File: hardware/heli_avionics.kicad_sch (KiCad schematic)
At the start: 17 parts, among them J1 Pin_Header_2x3, J7 JST_ZH_01x02, SW1 Reset, U1 ATmega4808-A

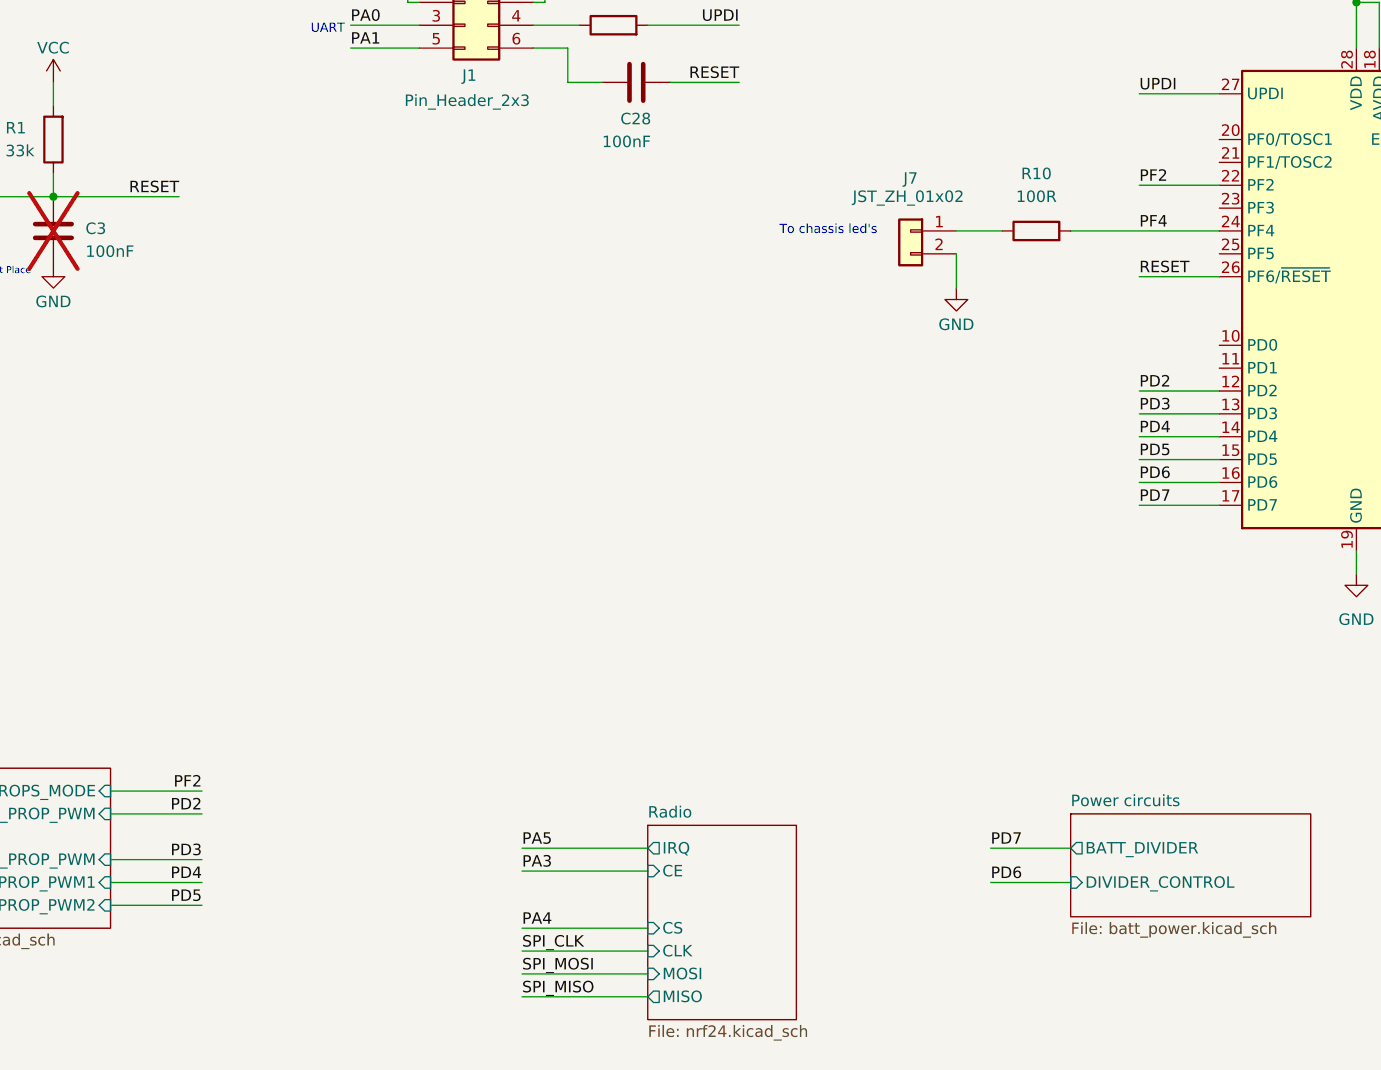
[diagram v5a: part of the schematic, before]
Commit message: Reordered some MCU pin connections for nicer layout
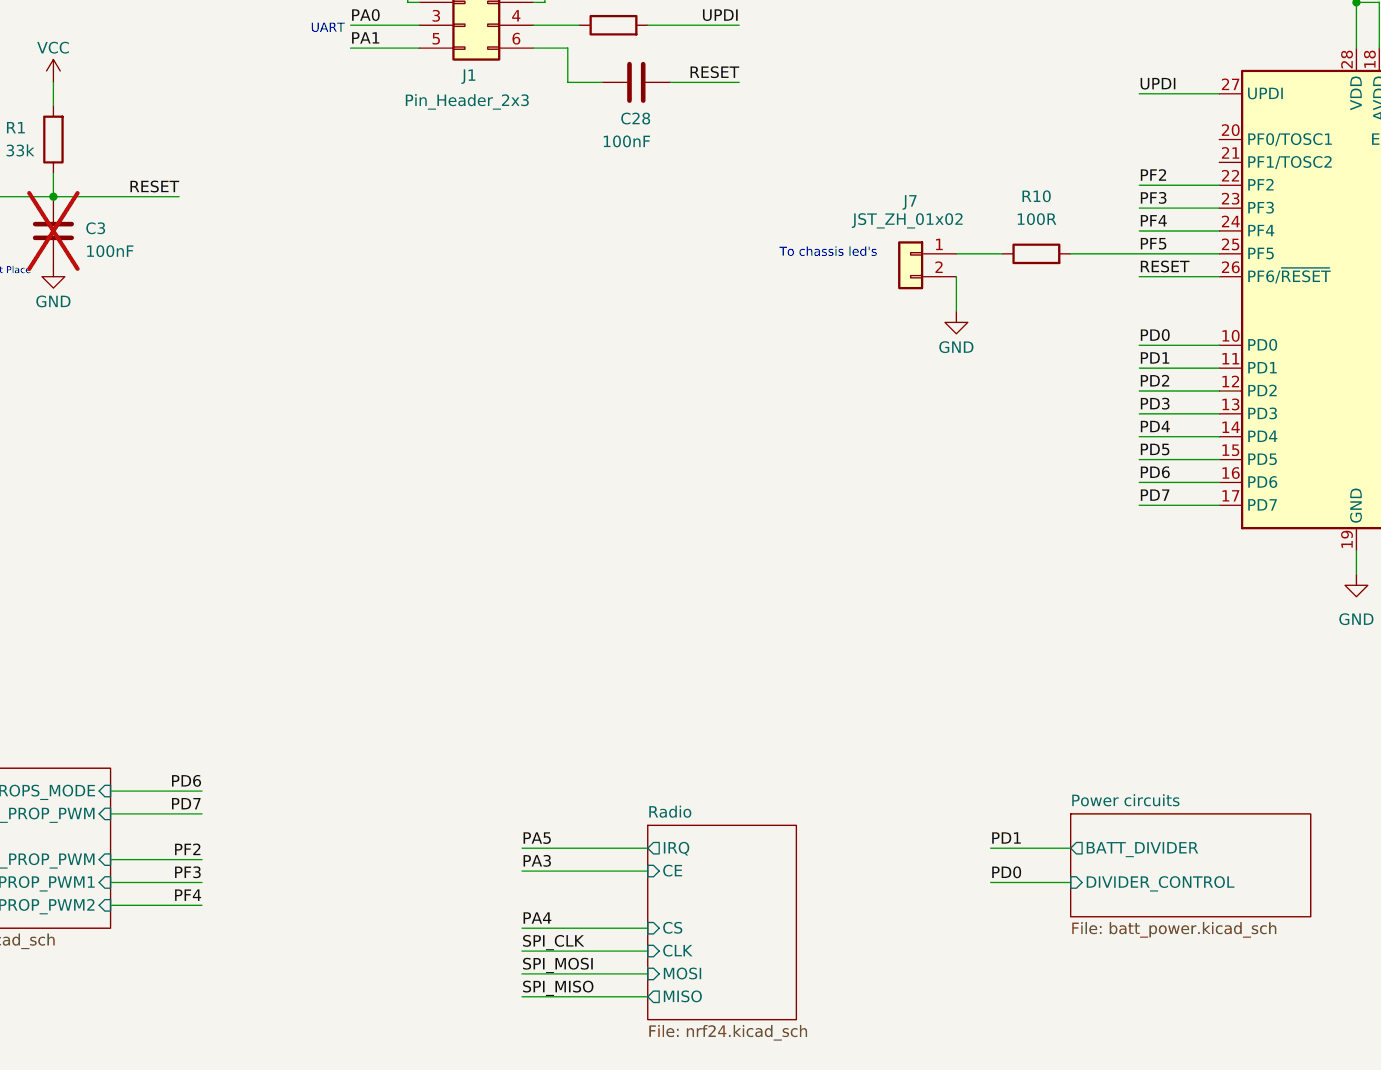
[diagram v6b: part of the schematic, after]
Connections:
- net PF4: no longer R10.2
- net PD0: now reaches U1.10 (PD0)
- net PD1: now reaches U1.11 (PD1)
- net PF3: now reaches U1.23 (PF3)
- net PF5: now reaches U1.25 (PF5)
- net PF5: now also R10.2
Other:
- moved on the sheet: J7, R10
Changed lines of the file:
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@@
+	(wire
+		(pts
+			(xy 181.61 68.58) (xy 190.5 68.58)
+		)
+		(stroke
+			(width 0)
+			(type default)
+		)
+	)
 	(wire
 		(pts
@@
 	(wire
 		(pts
+			(xy 181.61 83.82) (xy 190.5 83.82)
+		)
+		(stroke
+			(width 0)
+			(type default)
+		)
+	)
+	(wire
+		(pts
 			(xy 205.74 39.37) (xy 205.74 43.18)
 		)
@@
 	(wire
 		(pts
+			(xy 173.99 71.12) (xy 190.5 71.12)
+		)
+		(stroke
+			(width 0)
+			(type default)
+		)
+	)
+	(wire
+		(pts
 			(xy 68.58 180.34) (xy 81.28 180.34)
 		)
@@
 	(wire
 		(pts
+			(xy 181.61 66.04) (xy 190.5 66.04)
+		)
+		(stroke
+			(width 0)
+			(type default)
+		)
+	)
+	(wire
+		(pts
 			(xy 29.21 64.77) (xy 29.21 69.85)
 		)
@@
 	(wire
 		(pts
-			(xy 161.29 68.58) (xy 166.37 68.58)
+			(xy 161.29 71.12) (xy 166.37 71.12)
 		)
 		(stroke
@@
 	(wire
 		(pts
+			(xy 181.61 81.28) (xy 190.5 81.28)
+		)
+		(stroke
+			(width 0)
+			(type default)
+		)
+	)
+	(wire
+		(pts
 			(xy 205.74 43.18) (xy 208.28 43.18)
 		)
@@
 	(wire
 		(pts
-			(xy 161.29 71.12) (xy 161.29 74.93)
+			(xy 161.29 73.66) (xy 161.29 77.47)
 		)
 		(stroke
@@
 		(pts
 			(xy 181.61 96.52) (xy 190.5 96.52)
-		)
-		(stroke
-			(width 0)
-			(type default)
-		)
-	)
-	(wire
-		(pts
-			(xy 173.99 68.58) (xy 190.5 68.58)
 		)
 		(stroke
@@
 	(text "To chassis led's"
 		(exclude_from_sim no)
-		(at 147.066 68.58 0)
+		(at 147.066 71.12 0)
 		(effects
 			(font
@@
 		)
 	)
+	(label "PD0"
+		(at 165.1 140.97 0)
+		(fields_autoplaced yes)
+		(effects
+			(font
+				(size 1.27 1.27)
+			)
+			(justify left bottom)
+		)
+	)
 	(label "PF2"
 		(at 181.61 63.5 0)
@@
 		)
 	)
+	(label "PD1"
+		(at 181.61 83.82 0)
+		(fields_autoplaced yes)
+		(effects
+			(font
+				(size 1.27 1.27)
+			)
+			(justify left bottom)
+		)
+	)
 	(label "RESET"
 		(at 137.16 52.07 180)
@@
 		)
 	)
-	(label "PD4"
+	(label "PD1"
+		(at 165.1 137.16 0)
+		(fields_autoplaced yes)
+		(effects
+			(font
+				(size 1.27 1.27)
+			)
+			(justify left bottom)
+		)
+	)
+	(label "PF3"
 		(at 77.47 140.97 180)
 		(fields_autoplaced yes)
@@
 		)
 	)
-	(label "PD7"
-		(at 165.1 137.16 0)
-		(fields_autoplaced yes)
-		(effects
-			(font
-				(size 1.27 1.27)
-			)
-			(justify left bottom)
-		)
-	)
 	(label "PA4"
 		(at 113.03 146.05 0)
@@
 		)
 	)
-	(label "PD5"
+	(label "PF4"
 		(at 77.47 143.51 180)
 		(fields_autoplaced yes)
@@
 		)
 	)
+	(label "PF3"
+		(at 181.61 66.04 0)
+		(fields_autoplaced yes)
+		(effects
+			(font
+				(size 1.27 1.27)
+			)
+			(justify left bottom)
+		)
+	)
 	(label "PA0"
 		(at 232.41 58.42 180)
@@
 		)
 	)
+	(label "PF5"
+		(at 181.61 71.12 0)
+		(fields_autoplaced yes)
+		(effects
+			(font
+				(size 1.27 1.27)
+			)
+			(justify left bottom)
+		)
+	)
 	(label "PA3"
 		(at 113.03 139.7 0)
@@
 		)
 	)
-	(label "PF2"
+	(label "PD6"
 		(at 77.47 130.81 180)
 		(fields_autoplaced yes)
@@
 		)
 	)
-	(label "PD6"
-		(at 165.1 140.97 0)
-		(fields_autoplaced yes)
-		(effects
-			(font
-				(size 1.27 1.27)
-			)
-			(justify left bottom)
-		)
-	)
-	(label "PD2"
+	(label "PD7"
 		(at 77.47 133.35 180)
 		(fields_autoplaced yes)
@@
 		)
 	)
+	(label "PD0"
+		(at 181.61 81.28 0)
+		(fields_autoplaced yes)
+		(effects
+			(font
+				(size 1.27 1.27)
+			)
+			(justify left bottom)
+		)
+	)
 	(label "SPI_CLK"
 		(at 113.03 148.59 0)
@@
 		)
 	)
-	(label "PD3"
+	(label "PF2"
 		(at 77.47 138.43 180)
 		(fields_autoplaced yes)
@@
 	(symbol
 		(lib_id "Connector_Generic:Conn_01x02")
-		(at 156.21 68.58 0)
+		(at 156.21 71.12 0)
 		(mirror y)
 		(unit 1)
@@
 		(dnp no)
 		(property "Reference" "J7"
-			(at 156.21 62.738 0)
+			(at 156.21 65.278 0)
 			(effects
 				(font
@@
 		)
 		(property "Value" "JST_ZH_01x02"
-			(at 155.956 64.77 0)
+			(at 155.956 67.31 0)
 			(effects
 				(font
@@
 		)
 		(property "Footprint" "Connector_JST:JST_ZH_B2B-ZR_1x02_P1.50mm_Vertical"
-			(at 156.21 68.58 0)
+			(at 156.21 71.12 0)
 			(effects
 				(font
@@
 		)
 		(property "Datasheet" "~"
-			(at 156.21 68.58 0)
+			(at 156.21 71.12 0)
 			(effects
 				(font
@@
 		)
 		(property "Description" "Generic connector, single row, 01x02, script generated (kicad-library-utils/schlib/autogen/connector/)"
-			(at 156.21 68.58 0)
+			(at 156.21 71.12 0)
 			(effects
 				(font
@@
 	(symbol
 		(lib_id "Device:R")
-		(at 170.18 68.58 90)
+		(at 170.18 71.12 90)
 		(unit 1)
 		(exclude_from_sim no)
@@
 		(fields_autoplaced yes)
 		(property "Reference" "R10"
-			(at 170.18 62.23 90)
+			(at 170.18 64.77 90)
 			(effects
 				(font
@@
 		)
 		(property "Value" "100R"
-			(at 170.18 64.77 90)
+			(at 170.18 67.31 90)
 			(effects
 				(font
@@
 		)
 		(property "Footprint" "Resistor_SMD:R_0603_1608Metric_Pad0.98x0.95mm_HandSolder"
-			(at 170.18 70.358 90)
+			(at 170.18 72.898 90)
 			(effects
 				(font
@@
 		)
 		(property "Datasheet" "~"
-			(at 170.18 68.58 0)
+			(at 170.18 71.12 0)
 			(effects
 				(font
@@
 		)
 		(property "Description" "Resistor"
-			(at 170.18 68.58 0)
+			(at 170.18 71.12 0)
 			(effects
 				(font
@@
 	(symbol
 		(lib_id "power:GND")
-		(at 161.29 74.93 0)
+		(at 161.29 77.47 0)
 		(mirror y)
 		(unit 1)
@@
 		(dnp no)
 		(property "Reference" "#PWR052"
-			(at 161.29 81.28 0)
+			(at 161.29 83.82 0)
 			(effects
 				(font
@@
 		)
 		(property "Value" "GND"
-			(at 161.29 78.994 0)
+			(at 161.29 81.534 0)
 			(effects
 				(font
@@
 		)
 		(property "Footprint" ""
-			(at 161.29 74.93 0)
+			(at 161.29 77.47 0)
 			(effects
 				(font
@@
 		)
 		(property "Datasheet" ""
-			(at 161.29 74.93 0)
+			(at 161.29 77.47 0)
 			(effects
 				(font
@@
 		)
 		(property "Description" "Power symbol creates a global label with name \"GND\" , ground"
-			(at 161.29 74.93 0)
-			(effects
-				(font
+			(at 161.29 77.47 0)
+			(effects
+				(font

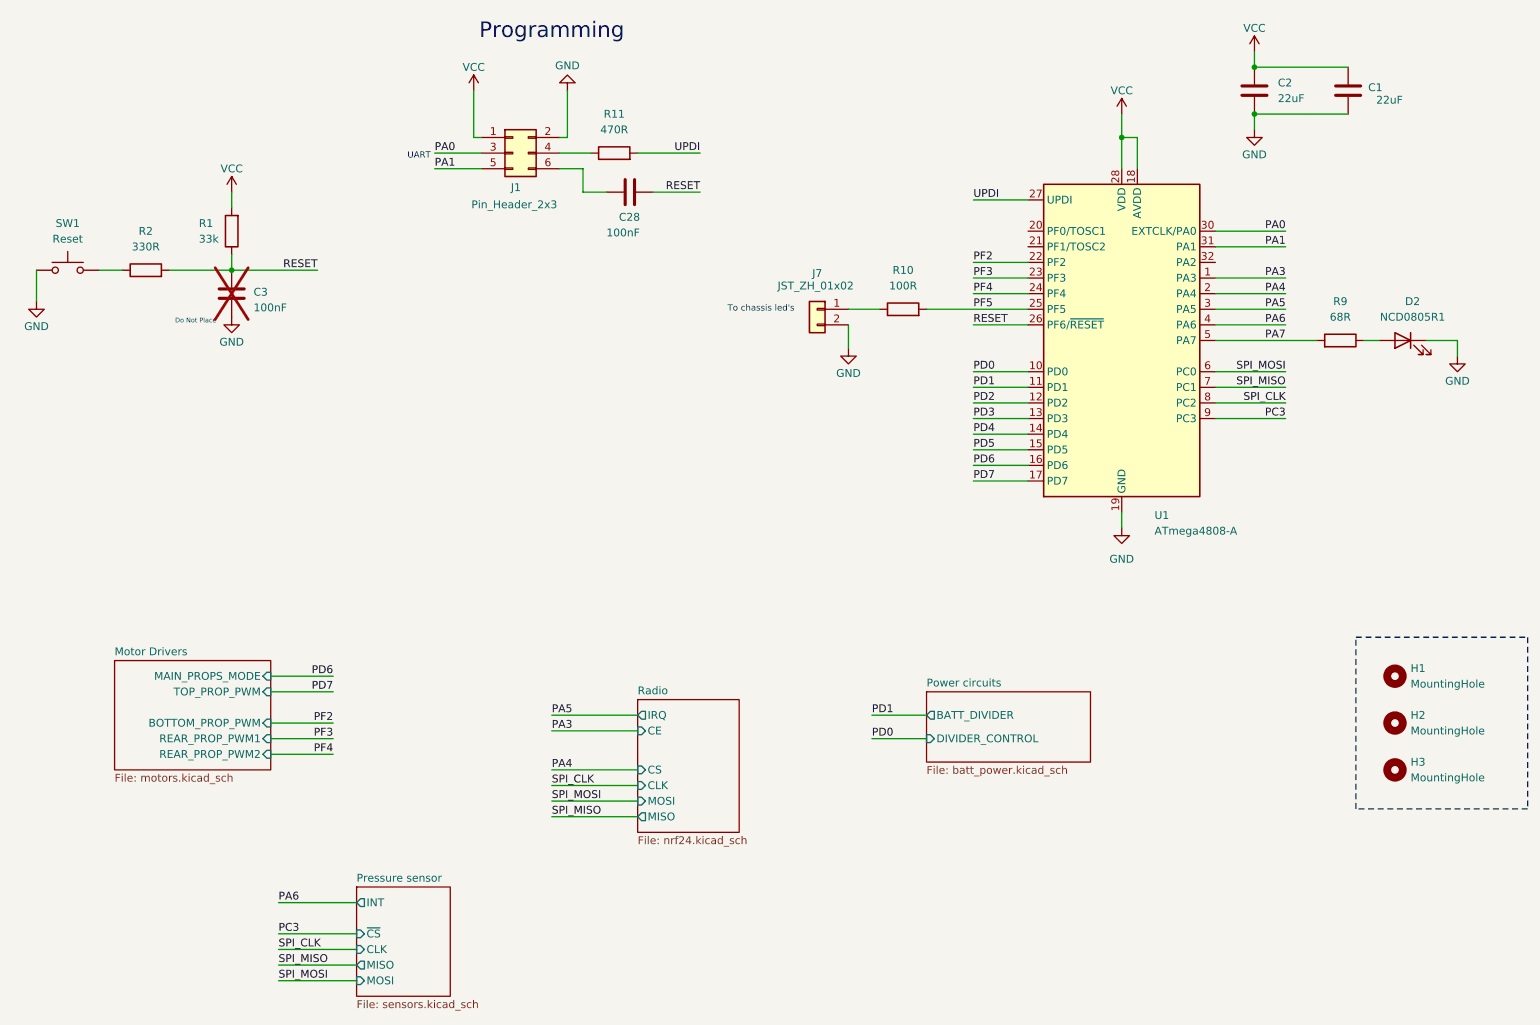
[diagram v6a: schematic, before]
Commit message: Pressure sensor now uses i2c
Also rewired nrf24 to use the other SPI
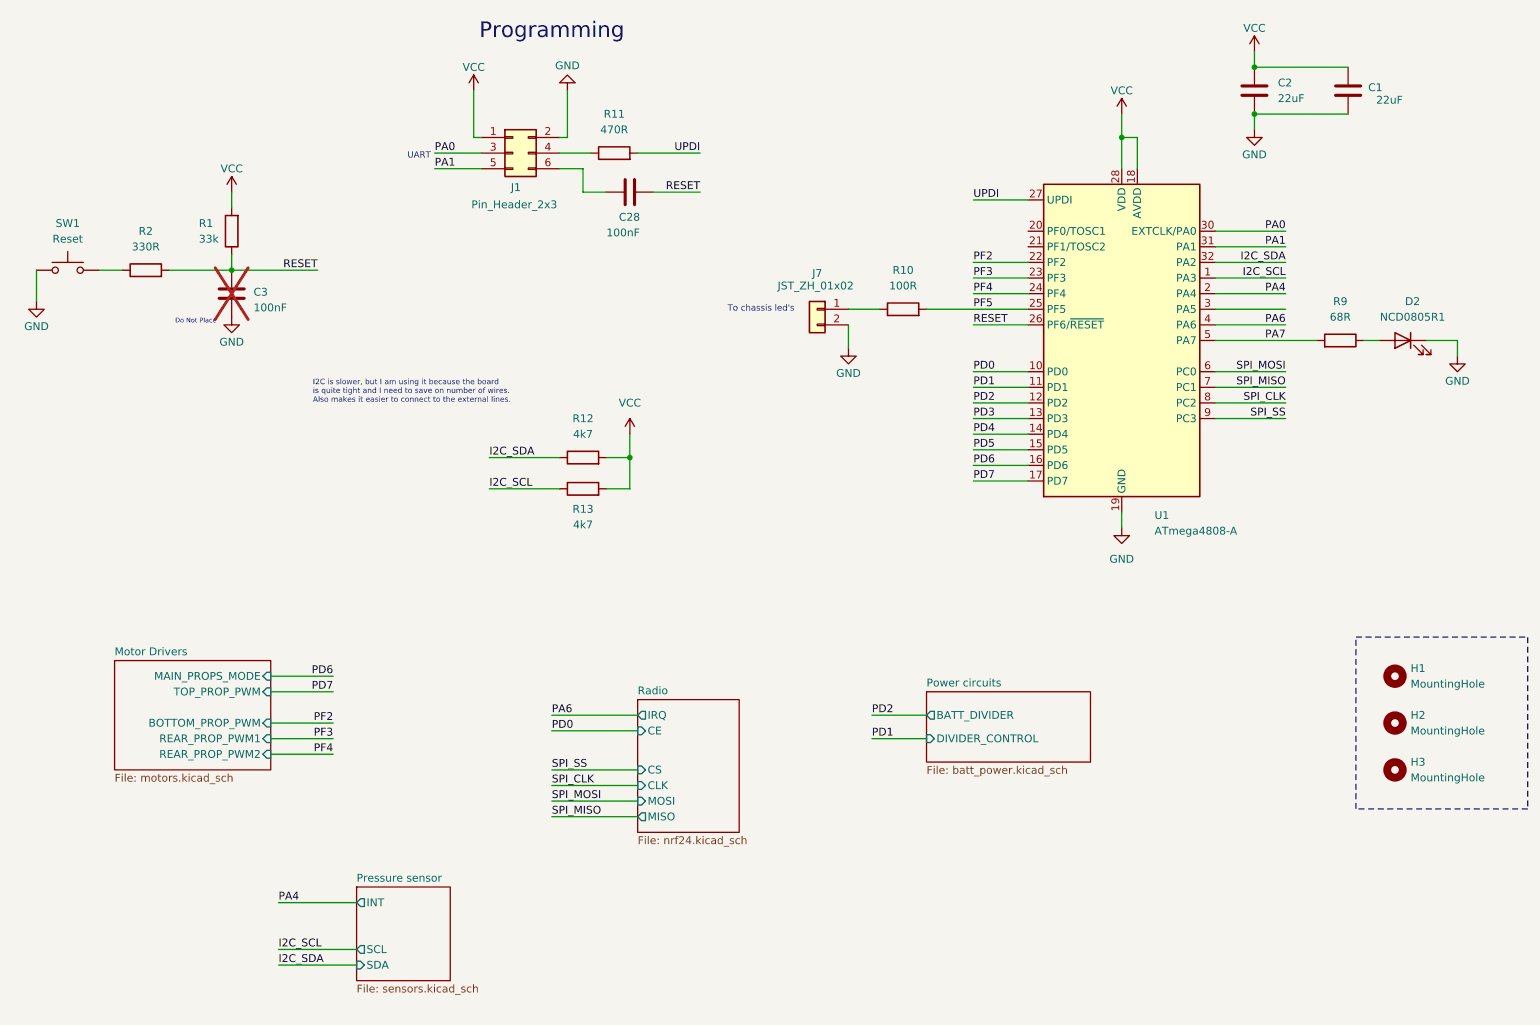
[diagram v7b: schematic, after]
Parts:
- added R12, R13: 4k7, Resistor_SMD:R_0603_1608Metric_Pad0.98x0.95mm_HandSolder, symbol Device:R
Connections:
- net VCC: now also R12.2, R13.2
- net I2C_SDA: now reaches U1.32 (PA2)
- net I2C_SDA: now also R12.1
- net PA3 renamed I2C_SCL
- net I2C_SCL: now also R13.1
- net PA5: no longer names the net of U1.3 (PA5)
- net PC3 renamed SPI_SS
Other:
- sheet Pressure sensor ports: added SCL, SDA; removed CLK, MISO, MOSI, ~{CS}
- note added: "I2C is slower, but I am using it because the board is quite tight and I need to save on number of wires. Also makes it easier to connect to the external lines."
